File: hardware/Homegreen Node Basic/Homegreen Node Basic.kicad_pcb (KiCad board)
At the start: 2 copper layers, 97 x 23.7 mm, 67 parts, among them J1 USB_B_Micro, J2 USB_A, J3 Conn_01x06_Pin, Q1 BC817DPN, Q2 BC817DPN, Q3 WST2011, SW1 SW_Push, U1 ATtiny88-A, U2 TM1637, U3 FJ3661BH, U4 TTP224, U5 MT3608, U6 INA180A2, U7 MT9700

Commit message: - starting with port to atmega328p
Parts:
- removed C9: 100n, Capacitor_SMD:C_0805_2012Metric
- removed U4: TTP224, Package_SO:SSOP-16_3.9x4.9mm_P0.635mm
- U1: value ATtiny88-A -> ATmega328PB
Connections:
- C10 pad 1: /User Interface/PAD_PLUS -> /BTN_PLUS
- C11 pad 1: /User Interface/PAD_SET -> /BTN_SET
- C12 pad 1: /User Interface/PAD_MINUS -> /BTN_MINUS
- C13 pad 1: /User Interface/PAD_MANUAL -> /BTN_MANUAL
- R1 pad 1: Net-(U1-PA0) -> Net-(R1-Pad1)
- R7 pad 2: Net-(U1-PA0) -> Net-(R1-Pad1)
- U1 pad 1: /BUT_MIN -> unconnected-(U1-PD3-Pad1)
- U1 pad 10: /TM_CLK -> unconnected-(U1-PD6-Pad10)
- U1 pad 11: /LED_ERR -> unconnected-(U1-PD7-Pad11)
- U1 pad 12: /USB2 -> unconnected-(U1-PB0-Pad12)
- U1 pad 13: /EN_CLK -> unconnected-(U1-PB1-Pad13)
- U1 pad 14: /LED_OK -> /USB2
- U1 pad 15: /MOSI -> /EN_CLK
- U1 pad 16: /MISO -> /LED_OK
- U1 pad 17: /SCK -> /MOSI
- U1 pad 19: Net-(U1-PA0) -> unconnected-(U1-PE2-Pad19)
- U1 pad 2: /BUT_MAN -> unconnected-(U1-PD4-Pad2)
- U1 pad 20: unconnected-(U1-PC7-Pad20) -> BAT_PWR
- U1 pad 22: /EN_PUMP -> unconnected-(U1-PE3-Pad22)
- U1 pad 23: /PUMP_VOL -> /BTN_LED
- U1 pad 24: /USB1 -> unconnected-(U1-PC1-Pad24)
- U1 pad 25: /~{EN_PB} -> /PUMP_VOL
- U1 pad 26: /PUMP_CURRENT -> /USB1
- U1 pad 27: /SDA -> /~{EN_PB}
- U1 pad 28: /SCL -> /PUMP_CURRENT
- U1 pad 3: /TOUCH_PWR -> unconnected-(U1-PE0-Pad3)
- U1 pad 30: /EN_LOAD -> unconnected-(U1-PD0-Pad30)
- U1 pad 31: /BUT_PLUS -> unconnected-(U1-PD1-Pad31)
- U1 pad 32: /BUT_SET -> unconnected-(U1-PD2-Pad32)
- U1 pad 7: unconnected-(U1-PB6-Pad7) -> /MISO
- U1 pad 8: /BTN_LED -> /SCK
- U1 pad 9: /TM_DIO -> unconnected-(U1-PD5-Pad9)
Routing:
- added copper zone on F.Cu, net /BTN_PLUS
- removed copper zone on F.Cu, net /User Interface/PAD_PLUS

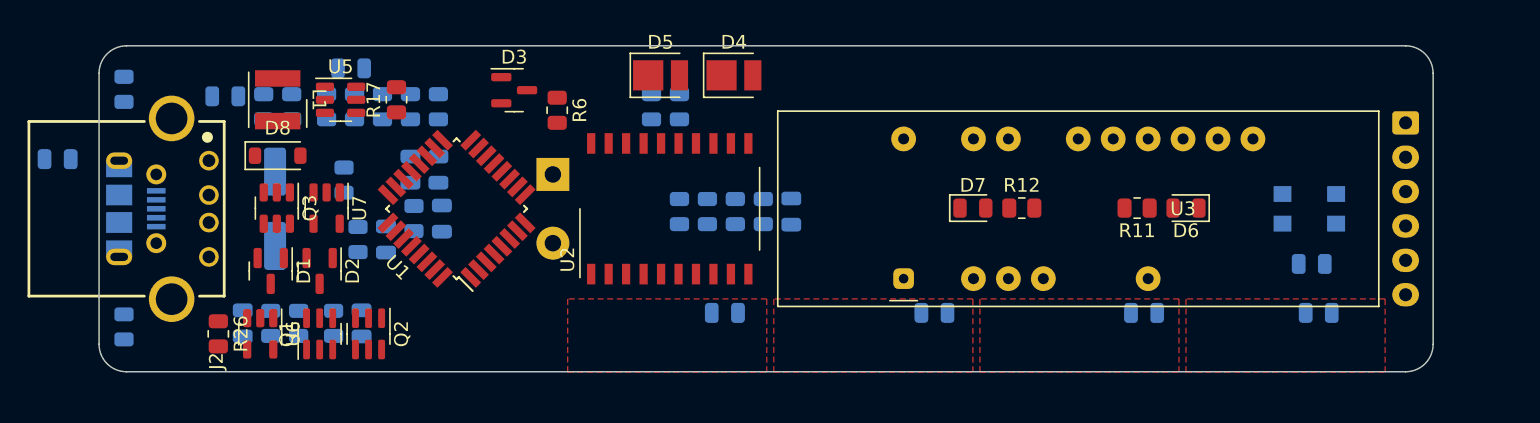
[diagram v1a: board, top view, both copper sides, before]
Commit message: update PCB to 1-sided for price estimation
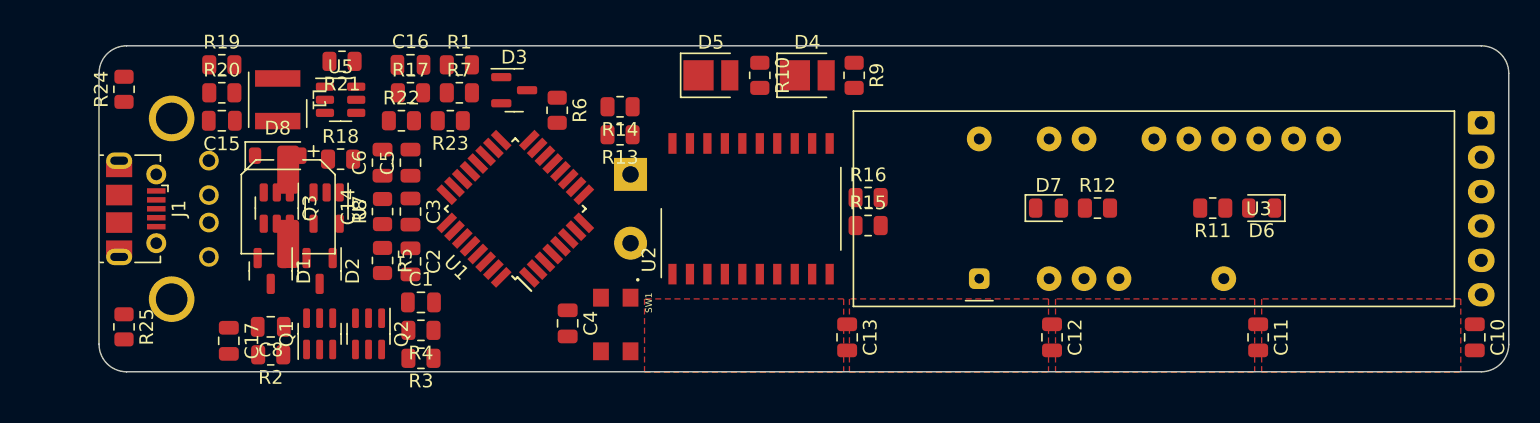
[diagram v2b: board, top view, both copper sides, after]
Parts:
- removed C18: 100n, Capacitor_SMD:C_0805_2012Metric
- removed R26: 20m, Resistor_SMD:R_0805_2012Metric
- removed U6: INA180A2, Package_TO_SOT_SMD:SOT-23-5
- C1, C10, C11, C12, C13, C14, C15, C16, C17, C2, C3, C4, C5, C6, C8, J1, R1, R10, R13, R14, R15, R16, R18, R19, R2, R20, R21, R22, R23, R24, R25, R3, R4, R5, R7, R8, R9, SW1: moved to F.Cu
- J2: moved to B.Cu
- moved C4 54.3 mm to (84.1, 170.2), turned to -90 degrees
- moved SW1 51.1 mm to (87.6, 170.3), turned to -90 degrees
- moved C17 18.1 mm to (59.4, 171.4), turned to -90 degrees
- moved R9 12.9 mm to (104.9, 152.1)
- moved C10 11.5 mm to (150.0, 171.2), turned to -90 degrees
- moved R14 9.92 mm to (87.9, 154.4), turned to 180 degrees
- moved R16 9.71 mm to (105.9, 161.0), turned to 0 degrees
- moved R3 9.25 mm to (73.4, 172.7), turned to 180 degrees
- moved C13 9.07 mm to (104.4, 171.2), turned to -90 degrees
- moved C12 8.73 mm to (119.3, 171.2), turned to -90 degrees
- moved C11 8.48 mm to (134.3, 171.2), turned to -90 degrees
- moved R10 8.20 mm to (98.0, 152.1)
- moved R15 7.69 mm to (105.9, 163.1), turned to 0 degrees
- moved R13 7.06 mm to (87.9, 156.5), turned to 180 degrees
- moved R4 6.37 mm to (73.4, 170.7), turned to 180 degrees
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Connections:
- J2 pad 4: Net-(J2-GND) -> unconnected-(J2-GND-Pad4)
- U1 pad 28: /PUMP_CURRENT -> unconnected-(U1-PC5-Pad28)
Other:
- board size 97 x 23.7 mm -> 102.5 x 23.7 mm
